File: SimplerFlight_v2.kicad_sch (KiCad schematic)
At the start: 0 parts

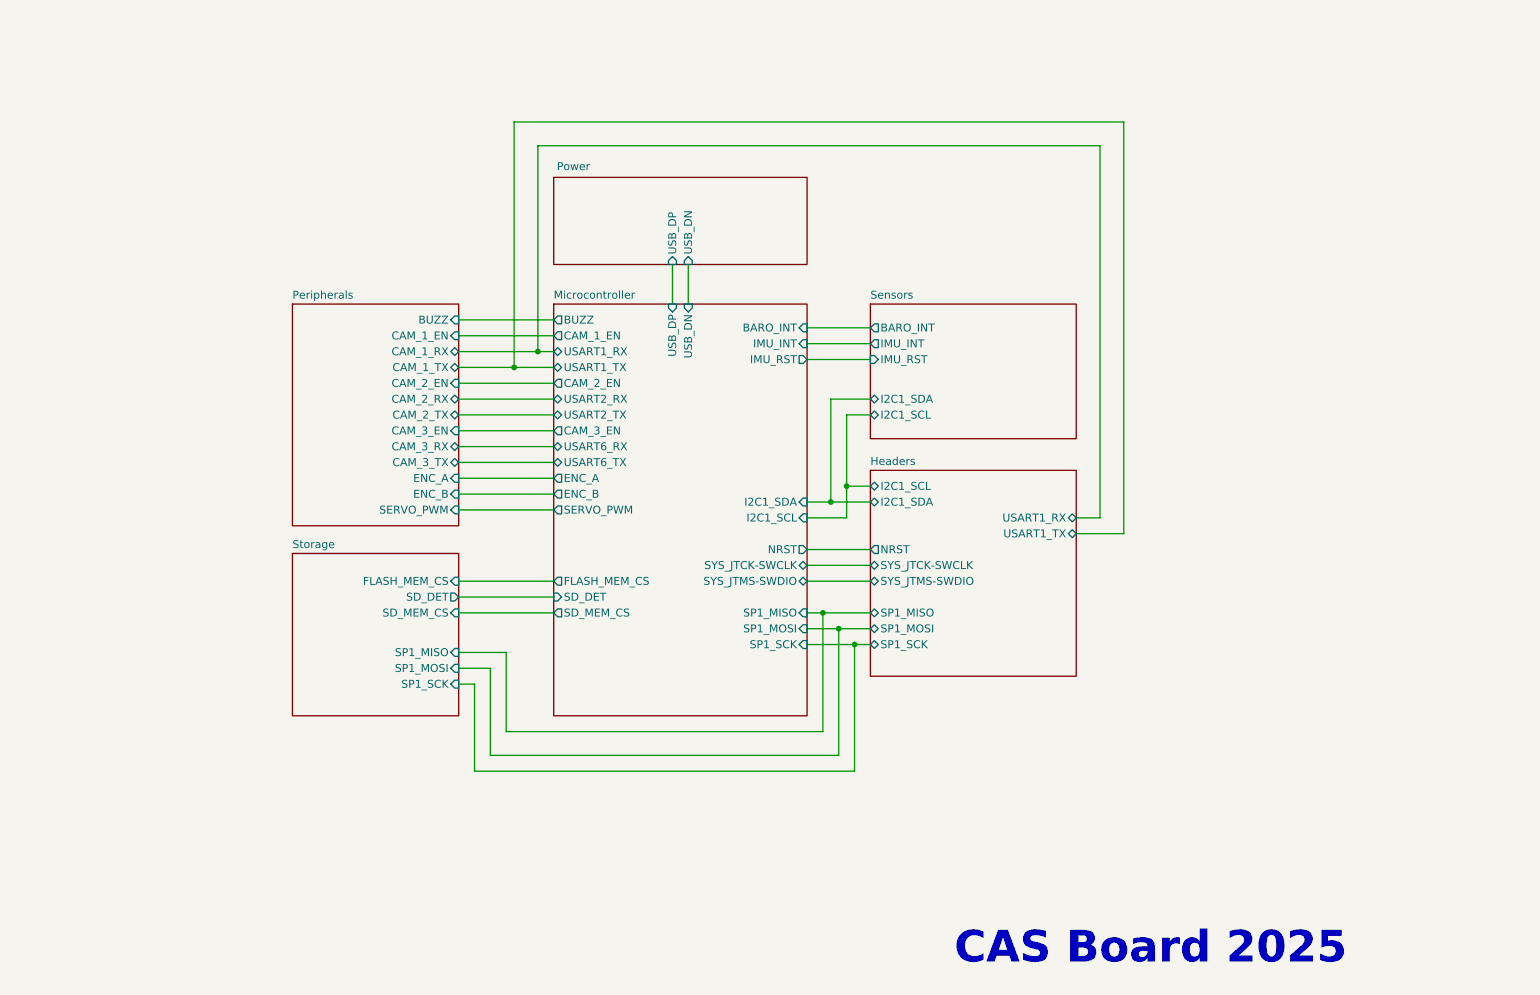
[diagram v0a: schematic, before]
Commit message: Added voltage/signal test points
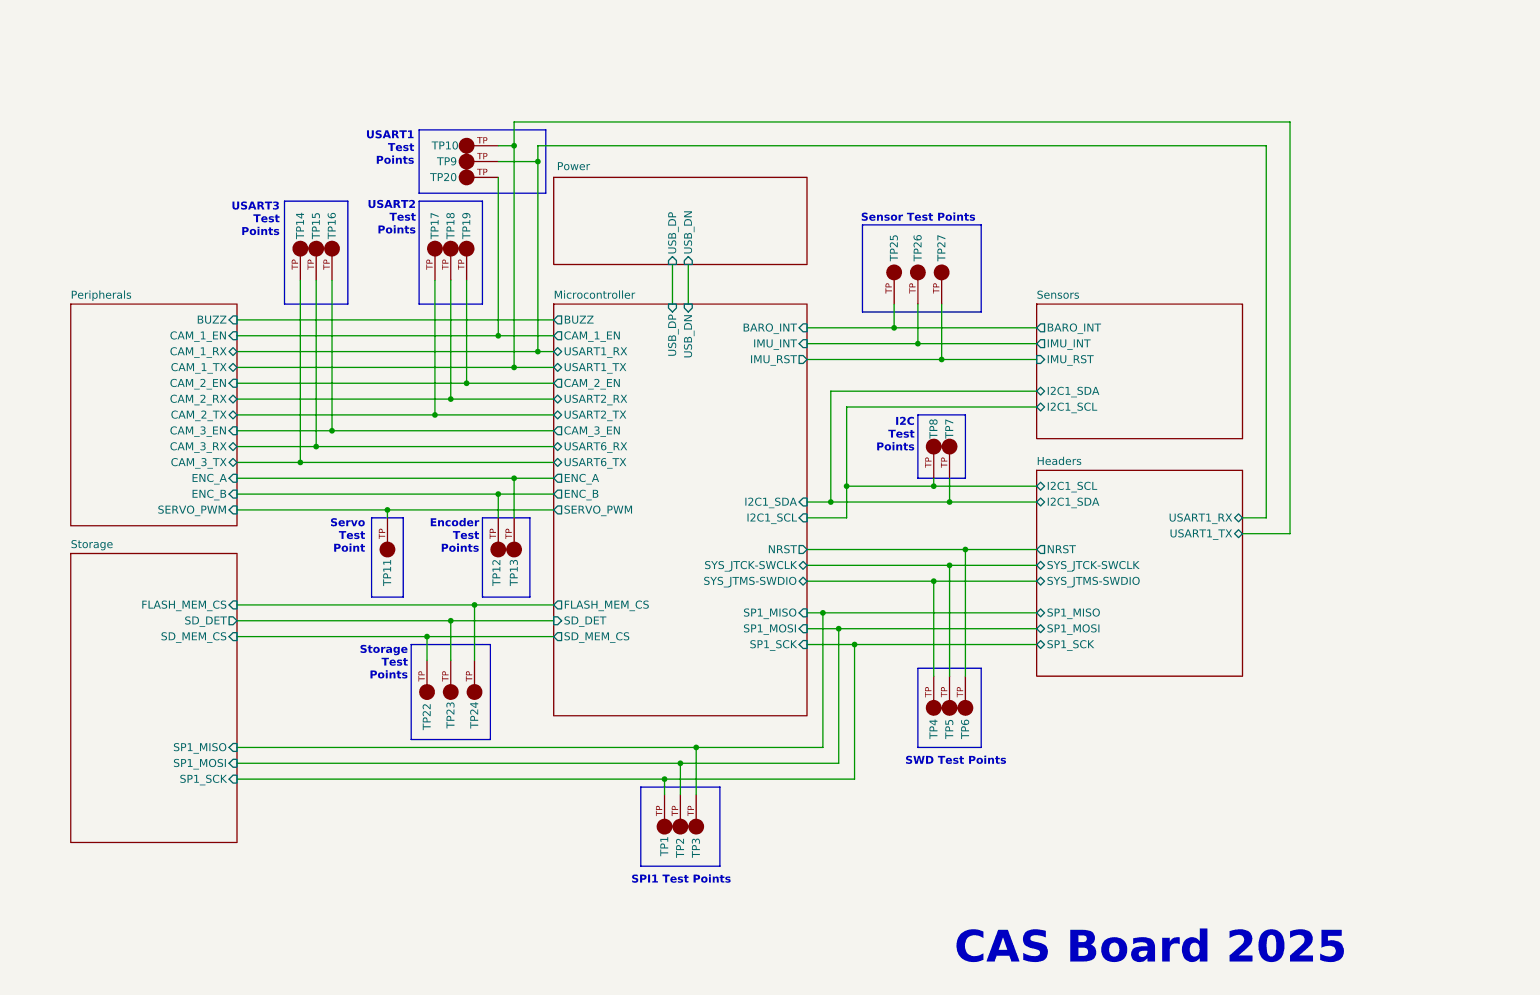
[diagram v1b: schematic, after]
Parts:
- added TP1, TP10, TP11, TP12, TP13, TP14, TP15, TP16, TP17, TP18, TP19, TP2, TP20, TP22, TP23, TP24, TP25, TP26, TP27, TP3, TP4, TP5, TP6, TP7, TP8, TP9: 5016, 5016:KEYSTONE_5016, symbol 5016:5016
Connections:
- net Headers/I2C1_SCL: now also TP8.TP
- net Headers/I2C1_SDA: now also TP7.TP
- net Headers/NRST: now also TP6.TP
- net Headers/SP1_MISO: now also TP3.TP
- net Headers/SP1_MOSI: now also TP2.TP
- net Headers/SP1_SCK: now also TP1.TP
- net Headers/SYS_JTCK-SWCLK: now also TP5.TP
- net Headers/SYS_JTMS-SWDIO: now also TP4.TP
- net Headers/USART1_RX: now also TP9.TP
- net Headers/USART1_TX: now also TP10.TP
- net Microcontroller/BARO_INT: now also TP25.TP
- net Microcontroller/CAM_1_EN: now also TP20.TP
- net Microcontroller/CAM_2_EN: now also TP19.TP
- net Microcontroller/CAM_3_EN: now also TP16.TP
- net Microcontroller/ENC_A: now also TP13.TP
- net Microcontroller/ENC_B: now also TP12.TP
- net Microcontroller/FLASH_MEM_CS: now also TP24.TP
- net Microcontroller/IMU_INT: now also TP26.TP
- net Microcontroller/IMU_RST: now also TP27.TP
- net Microcontroller/SD_DET: now also TP23.TP
- net Microcontroller/SD_MEM_CS: now also TP22.TP
- net Microcontroller/SERVO_PWM: now also TP11.TP
- net Microcontroller/USART2_RX: now also TP18.TP
- net Microcontroller/USART2_TX: now also TP17.TP
- net Microcontroller/USART6_RX: now also TP15.TP
- net Microcontroller/USART6_TX: now also TP14.TP
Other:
- note added: "Encoder Test Points"
- note added: "I2C Test Points"
- note added: "SPI1 Test Points"
- note added: "SWD Test Points"
- note added: "Sensor Test Points"
- note added: "Servo Test Point"
- note added: "Storage Test Points"
- note added: "USART1 Test Points"
- note added: "USART2 Test Points"
- note added: "USART3 Test Points"

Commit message: Initial layout for PCB components, updated README with images. Removed some test points and headers from final layout. Pending addition of buzzer. Pending additional power testing and pending routing.
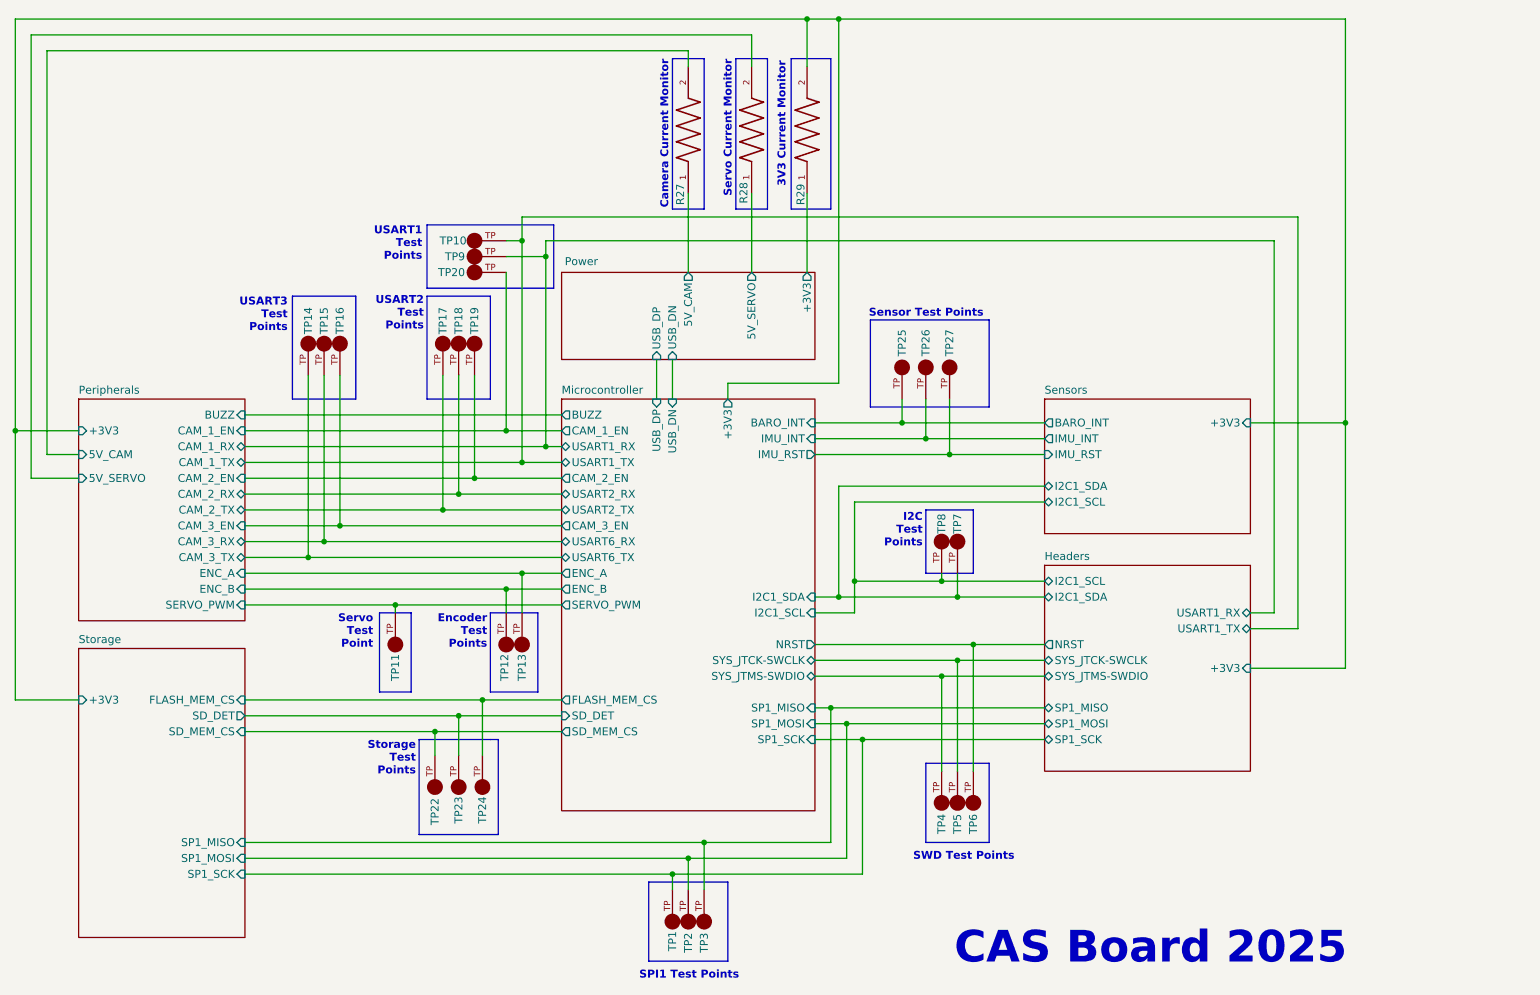
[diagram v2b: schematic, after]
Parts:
- added R27, R28, R29: CSRN2512FKR500, CSRN2512FKR500:RESC6331X70N, symbol CSRN2512FKR500:CSRN2512FKR500
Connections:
- new net Headers/+3V3: R29.2
- new net Peripherals/5V_CAM: R27.2
- new net Peripherals/5V_SERVO: R28.2
- new net Power/+3V3: R29.1
- new net Power/5V_CAM: R27.1
- new net Power/5V_SERVO: R28.1
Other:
- sheet Headers ports: added +3V3; removed none
- sheet Microcontroller ports: added +3V3; removed none
- sheet Peripherals ports: added +3V3, 5V_CAM, 5V_SERVO; removed none
- sheet Power ports: added +3V3, 5V_CAM, 5V_SERVO; removed none
- sheet Sensors ports: added +3V3; removed none
- sheet Storage ports: added +3V3; removed none
- note added: "3V3 Current Monitor"
- note added: "Camera Current Monitor"
- note added: "Servo Current Monitor"
- moved on the sheet: TP1, TP10, TP11, TP12, TP13, TP14, TP15, TP16, TP17, TP18, TP19, TP2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

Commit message: Layout
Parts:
- added H1, H2, H3, H4: MountingHole, MountingHole:MountingHole_3.2mm_M3, symbol Mechanical:MountingHole
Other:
- note added: "Mounting Holes"

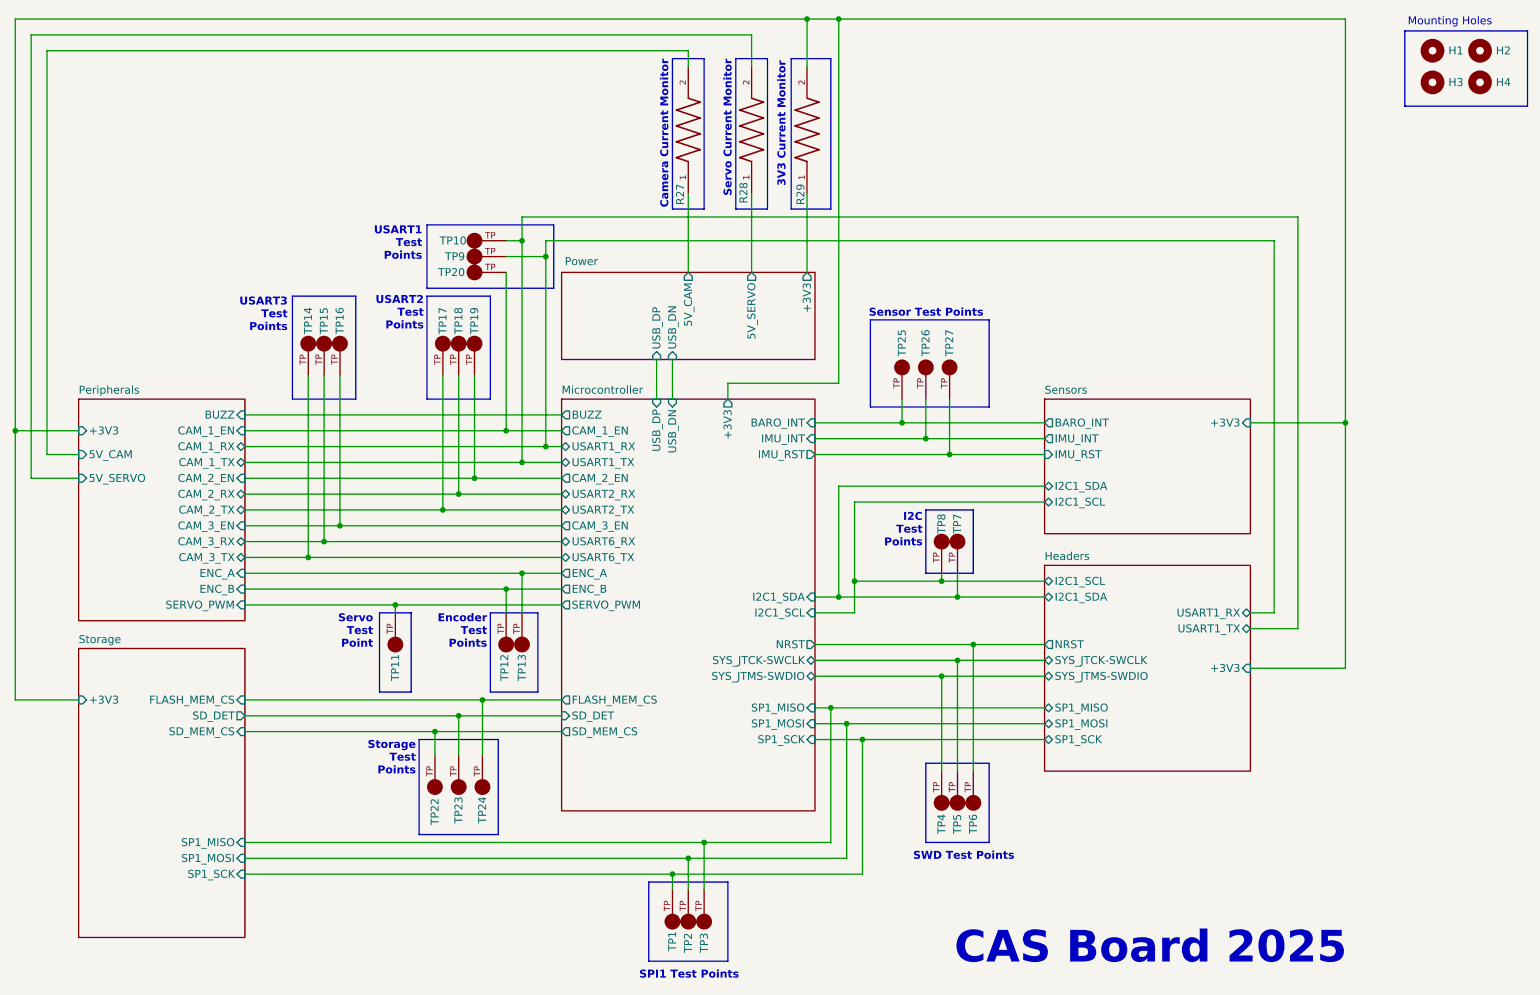
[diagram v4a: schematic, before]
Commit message: Removed uncvessary test points and headerrs. Added missing values. Update images of schematics
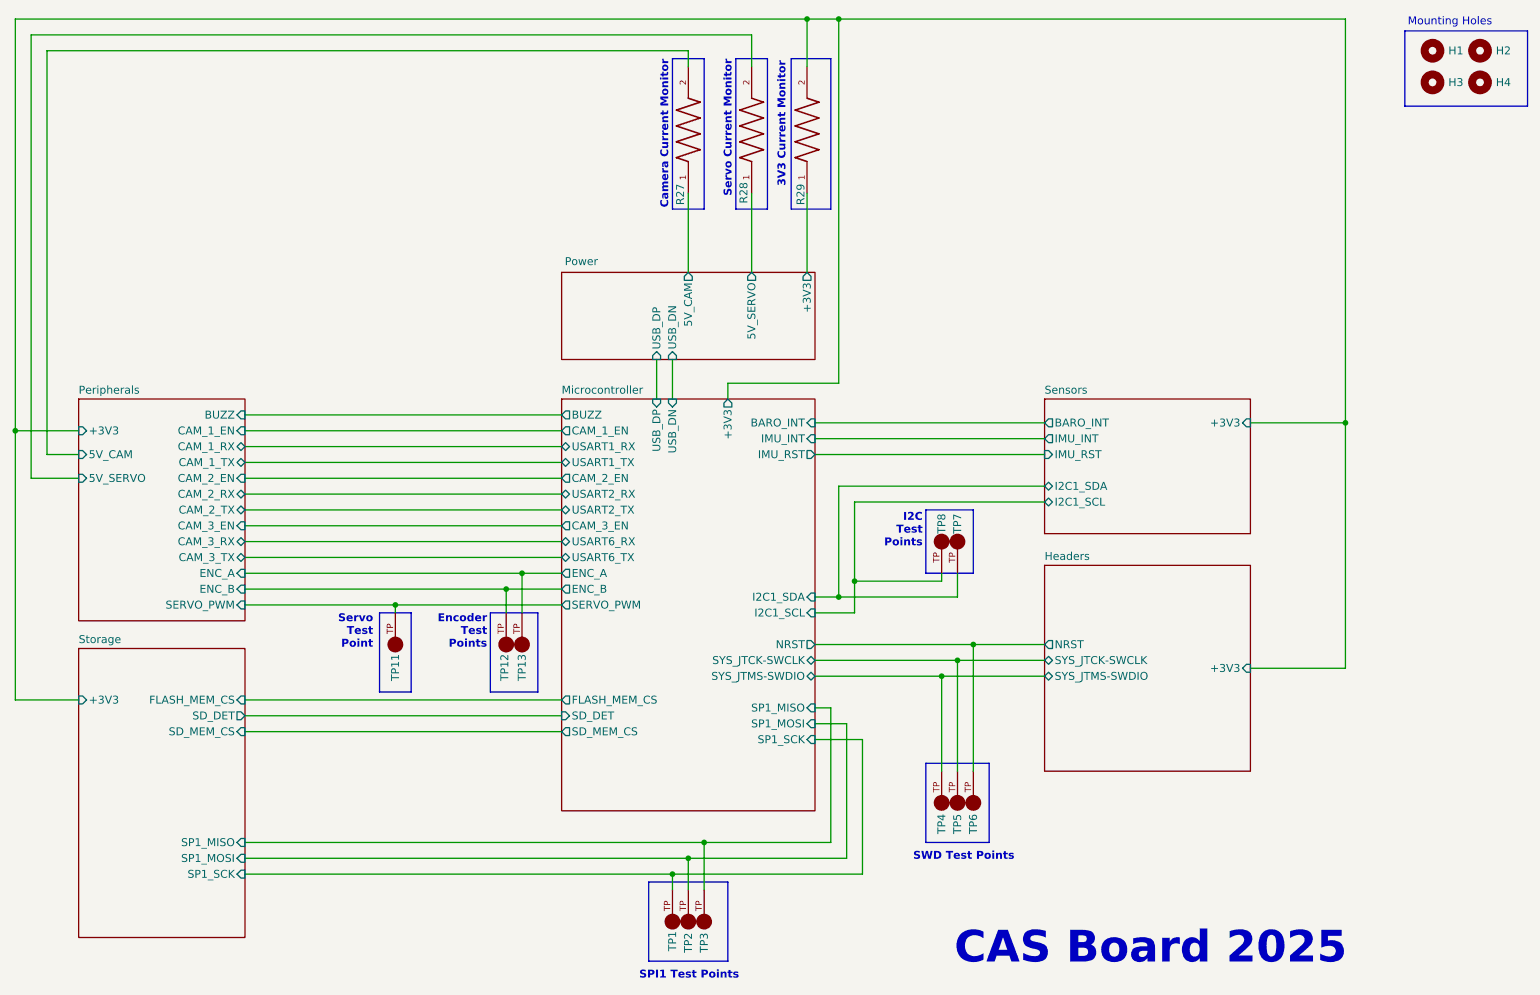
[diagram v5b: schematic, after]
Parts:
- removed TP10, TP14, TP15, TP16, TP17, TP18, TP19, TP20, TP22, TP23, TP24, TP25, TP26, TP27, TP9: 5016, 5016:KEYSTONE_5016, symbol 5016:5016
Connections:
- net Headers/I2C1_SCL renamed Microcontroller/I2C1_SCL
- net Headers/I2C1_SDA renamed Microcontroller/I2C1_SDA
- net Headers/SP1_MISO renamed Microcontroller/SP1_MISO
- net Headers/SP1_MOSI renamed Microcontroller/SP1_MOSI
- net Headers/SP1_SCK renamed Microcontroller/SP1_SCK
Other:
- sheet Headers ports: added none; removed I2C1_SCL, I2C1_SDA, SP1_MISO, SP1_MOSI, SP1_SCK, USART1_RX, USART1_TX
- note removed: "Sensor Test Points"
- note removed: "Storage Test Points"
- note removed: "USART1 Test Points"
- note removed: "USART2 Test Points"
- note removed: "USART3 Test Points"
